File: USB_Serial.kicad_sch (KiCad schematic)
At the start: 11 parts, among them J501 Header_Male_Pin_2.54mm_1X4_,_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, J502 690-005-299-043, U501 MCP2221A-I_SL

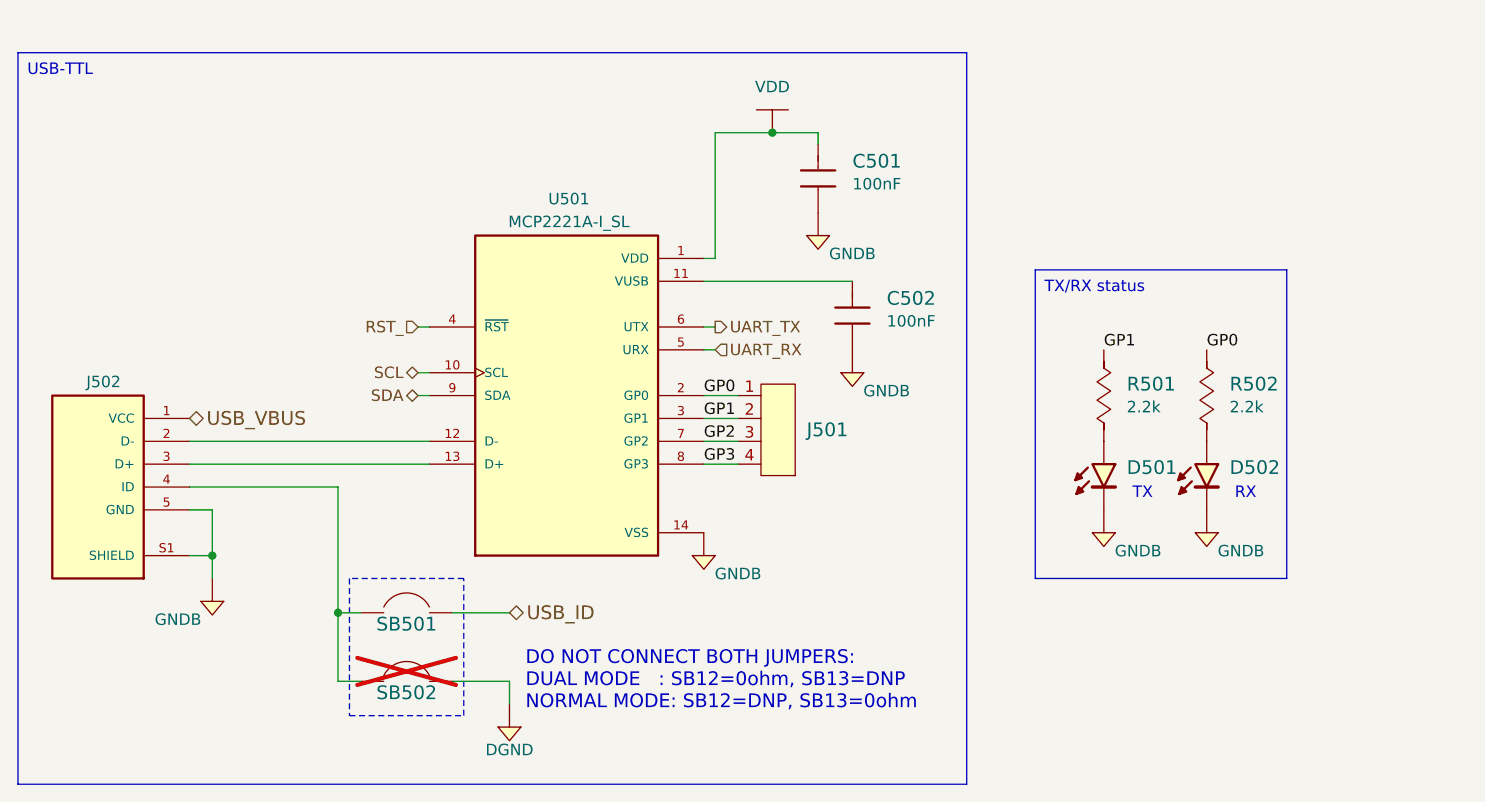
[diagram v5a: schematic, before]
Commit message: update schematic
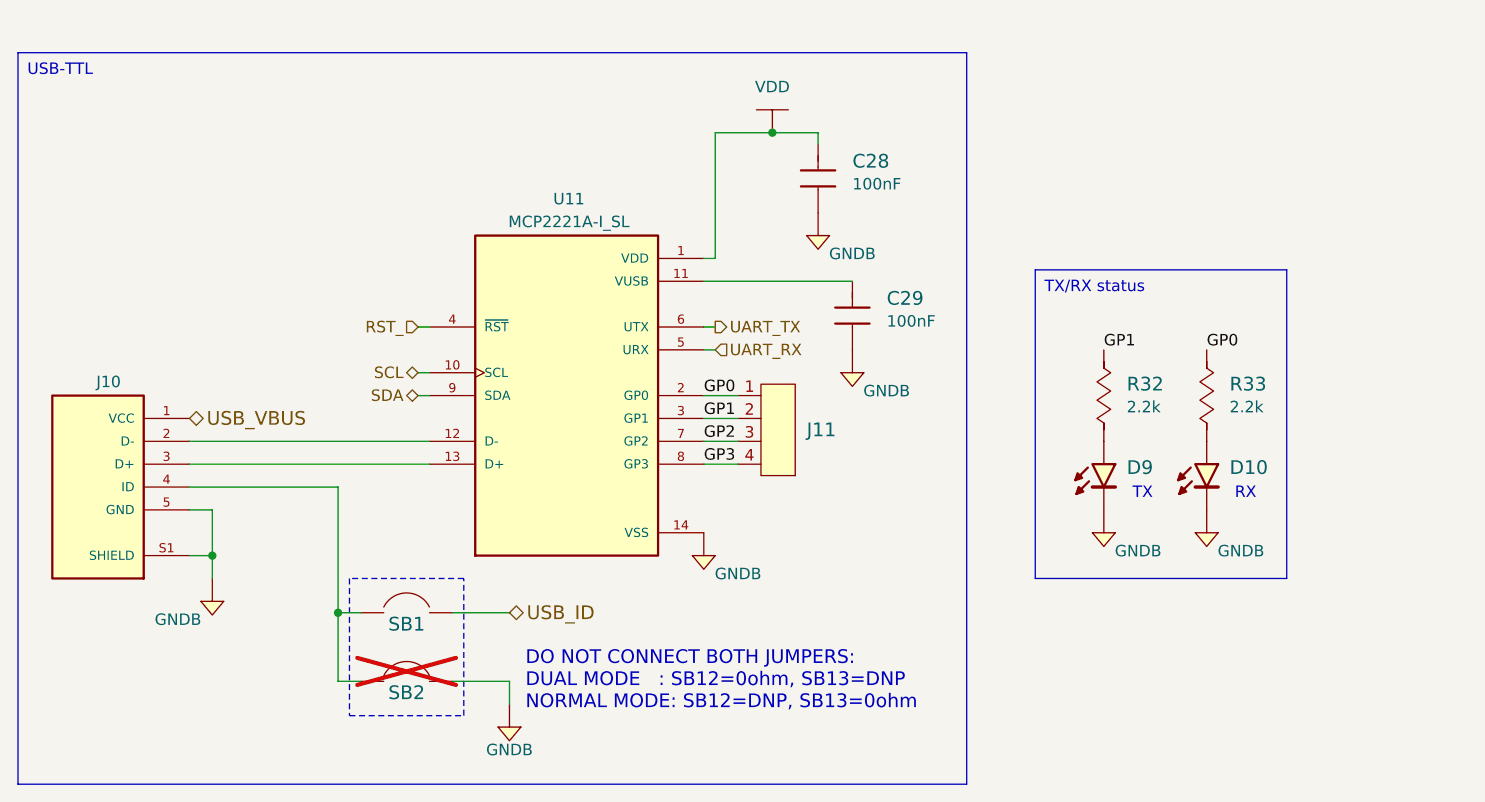
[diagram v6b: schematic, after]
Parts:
- renumbered C501 to C28, C502 to C29, D502 to D10, D501 to D9, J502 to J10, J501 to J11, R501 to R32, R502 to R33, SB501 to SB1, SB502 to SB2, U501 to U11
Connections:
- net DGND is gone; now on net GNDB: SB2.1
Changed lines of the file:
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@@
 		(on_board yes)
 		(dnp no)
-		(property "Reference" "#PWR0507"
+		(property "Reference" "#PWR086"
 			(at 86.36 110.998 0)
 			(effects
@@
 			(project "SACE-HW"
 				(path "/4c1e5ca8-aa0f-4a8e-bffe-6765adb2e3e8/9ebd2496-8213-4575-b78a-e0103001acbf"
-					(reference "#PWR0507")
+					(reference "#PWR086")
 					(unit 1)
 				)
@@
 		(dnp no)
 		(fields_autoplaced yes)
-		(property "Reference" "C501"
+		(property "Reference" "C28"
 			(at 157.48 57.7849 90)
 			(effects
@@
 			(project "SACE-HW"
 				(path "/4c1e5ca8-aa0f-4a8e-bffe-6765adb2e3e8/9ebd2496-8213-4575-b78a-e0103001acbf"
-					(reference "C501")
+					(reference "C28")
 					(unit 1)
 				)
@@
 		(dnp no)
 		(fields_autoplaced yes)
-		(property "Reference" "D501"
+		(property "Reference" "D9"
 			(at 187.96 91.8209 90)
 			(effects
@@
 			(project "SACE-HW"
 				(path "/4c1e5ca8-aa0f-4a8e-bffe-6765adb2e3e8/9ebd2496-8213-4575-b78a-e0103001acbf"
-					(reference "D501")
+					(reference "D9")
 					(unit 1)
 				)
@@
 		(dnp no)
 		(fields_autoplaced yes)
-		(property "Reference" "J501"
+		(property "Reference" "J11"
 			(at 152.4 87.6299 0)
 			(effects
@@
 			(project "SACE-HW"
 				(path "/4c1e5ca8-aa0f-4a8e-bffe-6765adb2e3e8/9ebd2496-8213-4575-b78a-e0103001acbf"
-					(reference "J501")
+					(reference "J11")
 					(unit 1)
 				)
@@
 		(on_board yes)
 		(dnp no)
-		(property "Reference" "#PWR0502"
+		(property "Reference" "#PWR090"
 			(at 153.67 70.358 0)
 			(effects
@@
 			(project "SACE-HW"
 				(path "/4c1e5ca8-aa0f-4a8e-bffe-6765adb2e3e8/9ebd2496-8213-4575-b78a-e0103001acbf"
-					(reference "#PWR0502")
+					(reference "#PWR090")
 					(unit 1)
 				)
@@
 		(on_board yes)
 		(dnp no)
-		(property "Reference" "#PWR0505"
+		(property "Reference" "#PWR093"
 			(at 196.85 103.378 0)
 			(effects
@@
 			(project "SACE-HW"
 				(path "/4c1e5ca8-aa0f-4a8e-bffe-6765adb2e3e8/9ebd2496-8213-4575-b78a-e0103001acbf"
-					(reference "#PWR0505")
+					(reference "#PWR093")
 					(unit 1)
 				)
@@
 		(dnp no)
 		(fields_autoplaced yes)
-		(property "Reference" "#PWR0501"
+		(property "Reference" "#PWR089"
 			(at 148.59 58.42 0)
 			(effects
@@
 			(project "SACE-HW"
 				(path "/4c1e5ca8-aa0f-4a8e-bffe-6765adb2e3e8/9ebd2496-8213-4575-b78a-e0103001acbf"
-					(reference "#PWR0501")
+					(reference "#PWR089")
 					(unit 1)
 				)
@@
 		(on_board yes)
 		(dnp yes)
-		(property "Reference" "SB502"
+		(property "Reference" "SB2"
 			(at 107.95 116.84 0)
 			(effects
@@
 			(project "SACE-HW"
 				(path "/4c1e5ca8-aa0f-4a8e-bffe-6765adb2e3e8/9ebd2496-8213-4575-b78a-e0103001acbf"
-					(reference "SB502")
+					(reference "SB2")
 					(unit 1)
 				)
@@
 		(dnp no)
 		(fields_autoplaced yes)
-		(property "Reference" "R502"
+		(property "Reference" "R33"
 			(at 199.39 82.5499 90)
 			(effects
@@
 			(project "SACE-HW"
 				(path "/4c1e5ca8-aa0f-4a8e-bffe-6765adb2e3e8/9ebd2496-8213-4575-b78a-e0103001acbf"
-					(reference "R502")
+					(reference "R33")
 					(unit 1)
 				)
@@
 		(on_board yes)
 		(dnp no)
-		(property "Reference" "#PWR0506"
+		(property "Reference" "#PWR088"
 			(at 140.97 105.918 0)
 			(effects
@@
 			(project "SACE-HW"
 				(path "/4c1e5ca8-aa0f-4a8e-bffe-6765adb2e3e8/9ebd2496-8213-4575-b78a-e0103001acbf"
-					(reference "#PWR0506")
+					(reference "#PWR088")
 					(unit 1)
 				)
@@
 		(dnp no)
 		(fields_autoplaced yes)
-		(property "Reference" "C502"
+		(property "Reference" "C29"
 			(at 161.29 73.0249 90)
 			(effects
@@
 			(project "SACE-HW"
 				(path "/4c1e5ca8-aa0f-4a8e-bffe-6765adb2e3e8/9ebd2496-8213-4575-b78a-e0103001acbf"
-					(reference "C502")
+					(reference "C29")
 					(unit 1)
 				)
@@
 		(on_board yes)
 		(dnp no)
-		(property "Reference" "#PWR0504"
+		(property "Reference" "#PWR092"
 			(at 185.42 103.378 0)
 			(effects
@@
 			(project "SACE-HW"
 				(path "/4c1e5ca8-aa0f-4a8e-bffe-6765adb2e3e8/9ebd2496-8213-4575-b78a-e0103001acbf"
-					(reference "#PWR0504")
+					(reference "#PWR092")
 					(unit 1)
 				)
@@
 		(on_board yes)
 		(dnp no)
-		(property "Reference" "#PWR0503"
+		(property "Reference" "#PWR091"
 			(at 157.48 85.598 0)
 			(effects
@@
 			(project "SACE-HW"
 				(path "/4c1e5ca8-aa0f-4a8e-bffe-6765adb2e3e8/9ebd2496-8213-4575-b78a-e0103001acbf"
-					(reference "#PWR0503")
+					(reference "#PWR091")
 					(unit 1)
 				)
@@
 	)
 	(symbol
-		(lib_id "Power_Port:DGND")
+		(lib_id "Power_Port:GNDB")
 		(at 119.38 120.65 0)
 		(mirror y)
@@
 		(on_board yes)
 		(dnp no)
-		(property "Reference" "#PWR0508"
+		(property "Reference" "#PWR087"
 			(at 119.38 124.968 0)
 			(effects
@@
 			)
 		)
-		(property "Value" "DGND"
+		(property "Value" "GNDB"
 			(at 119.38 123.19 0)
 			(effects
@@
 			(project "SACE-HW"
 				(path "/4c1e5ca8-aa0f-4a8e-bffe-6765adb2e3e8/9ebd2496-8213-4575-b78a-e0103001acbf"
-					(reference "#PWR0508")
+					(reference "#PWR087")
 					(unit 1)
 				)
@@
 		(on_board yes)
 		(dnp no)
-		(property "Reference" "J502"
+		(property "Reference" "J10"
 			(at 76.2 82.296 0)
 			(effects
@@
 			(project "SACE-HW"
 				(path "/4c1e5ca8-aa0f-4a8e-bffe-6765adb2e3e8/9ebd2496-8213-4575-b78a-e0103001acbf"
-					(reference "J502")
+					(reference "J10")
 					(unit 1)
 				)
@@
 		(on_board yes)
 		(dnp no)
-		(property "Reference" "SB501"
+		(property "Reference" "SB1"
 			(at 107.95 109.22 0)
 			(effects
@@
 			(project "SACE-HW"
 				(path "/4c1e5ca8-aa0f-4a8e-bffe-6765adb2e3e8/9ebd2496-8213-4575-b78a-e0103001acbf"
-					(reference "SB501")
+					(reference "SB1")
 					(unit 1)
 				)
@@
 		(dnp no)
 		(fields_autoplaced yes)
-		(property "Reference" "D502"
+		(property "Reference" "D10"
 			(at 199.39 91.8209 90)
 			(effects
@@
 			(project "SACE-HW"
 				(path "/4c1e5ca8-aa0f-4a8e-bffe-6765adb2e3e8/9ebd2496-8213-4575-b78a-e0103001acbf"
-					(reference "D502")
+					(reference "D10")
 					(unit 1)
 				)
@@
 		(on_board yes)
 		(dnp no)
-		(property "Reference" "U501"
+		(property "Reference" "U11"
 			(at 125.984 61.976 0)
 			(effects
@@
 			(project "SACE-HW"
 				(path "/4c1e5ca8-aa0f-4a8e-bffe-6765adb2e3e8/9ebd2496-8213-4575-b78a-e0103001acbf"
-					(reference "U501")
+					(reference "U11")
 					(unit 1)
 				)
@@
 		(dnp no)
 		(fields_autoplaced yes)
-		(property "Reference" "R501"
+		(property "Reference" "R32"
 			(at 187.96 82.5499 90)
 			(effects
@@
 			(project "SACE-HW"
 				(path "/4c1e5ca8-aa0f-4a8e-bffe-6765adb2e3e8/9ebd2496-8213-4575-b78a-e0103001acbf"
-					(reference "R501")
-					(unit 1)
-				)
+					(reference "R32")
+					(unit 1)
+				)

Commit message: finalisation de la schématique
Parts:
- removed SB1, SB2: Solder_Bridge, Connectors:Solder_bridge_0805, symbol Connectors:Solder_Bridge
- added R501: RC0805JR-07470RL, Resistors:R0805, symbol Resistors:RC0805JR-07470RL
- renumbered C28 to C501, C29 to C502, D9 to D501, D10 to D502, J11 to J501, J10 to J502, R32 to R502, R33 to R503, U11 to U501
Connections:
- net USB_VBUS: now also R501.2; no longer J502.1 (VCC)
- net USB_N: now reaches J502.2 (D-), U501.12 (D-)
- net USB_P: now reaches J502.3 (D+), U501.13 (D+)
- net VDD renamed 5VB
- new net: J502.1 (VCC), R501.1
- no-connect marks 0 -> 1
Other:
- note removed: "DO NOT CONNECT BOTH JUMPERS: DUAL MODE : SB12=0ohm, SB13=DNP NORMAL MODE: SB12=DNP, SB13=0ohm"
